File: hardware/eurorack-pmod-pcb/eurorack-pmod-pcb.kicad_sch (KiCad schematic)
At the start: 34 parts, among them J1 OPTIONAL, J2 PMOD, J3 EURORACK_PWR, U1 LM1117-3.3, U2 TL072, U3 AK4619VN

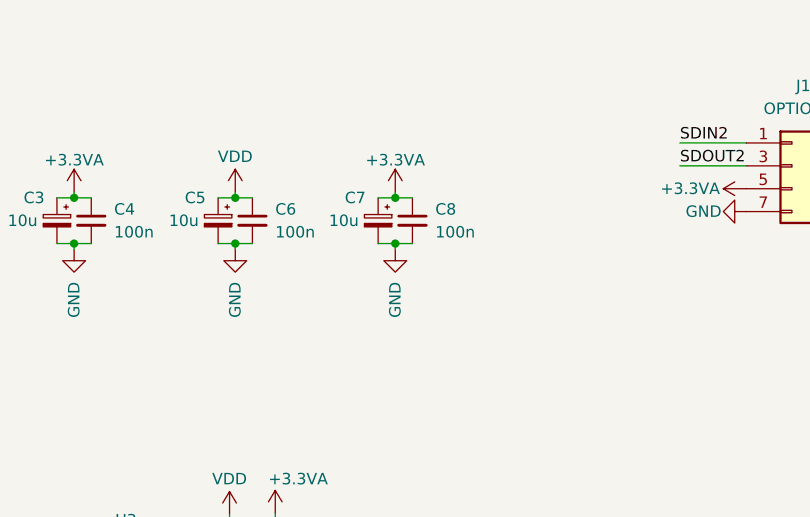
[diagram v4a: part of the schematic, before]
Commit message: Position all components on PCB
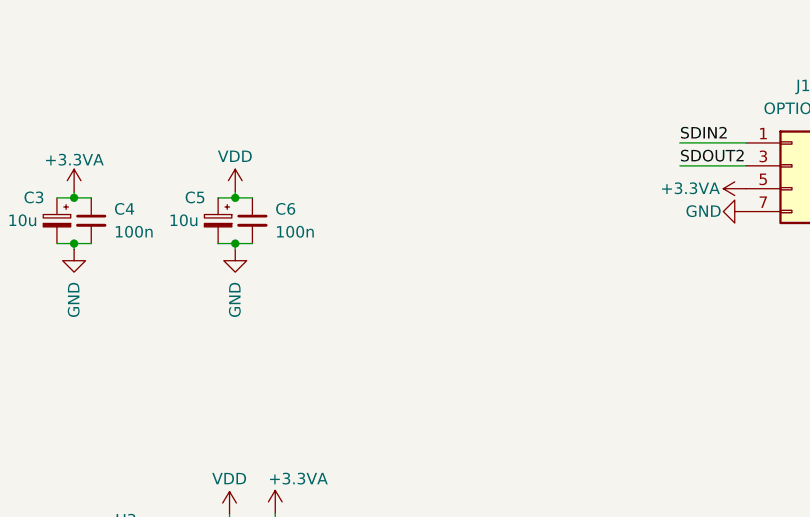
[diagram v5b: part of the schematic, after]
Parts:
- removed C7: 10u, Capacitor_Tantalum_SMD:CP_EIA-3216-10_Kemet-I, symbol Device:C_Polarized_Small
- removed C8: 100n, Capacitor_SMD:C_0603_1608Metric, symbol Device:C_Small
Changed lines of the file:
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@@
   (junction (at 247.015 88.9) (diameter 0) (color 0 0 0 0)
-  )
-  (junction (at 116.078 41.656) (diameter 0) (color 0 0 0 0)
-  )
-  (junction (at 116.078 36.576) (diameter 0) (color 0 0 0 0)
   )
   (junction (at 98.298 36.576) (diameter 0) (color 0 0 0 0)
@@
     (stroke (width 0) (type default) (color 0 0 0 0))
   )
-  (wire (pts (xy 116.078 41.656) (xy 117.983 41.656))
-    (stroke (width 0) (type default) (color 0 0 0 0))
-  )
   (wire (pts (xy 36.703 90.043) (xy 30.988 90.043))
     (stroke (width 0) (type default) (color 0 0 0 0))
@@
     (stroke (width 0) (type default) (color 0 0 0 0))
   )
-  (wire (pts (xy 116.078 41.656) (xy 116.078 42.291))
-    (stroke (width 0) (type default) (color 0 0 0 0))
-  )
   (wire (pts (xy 193.675 83.82) (xy 203.2 83.82))
     (stroke (width 0) (type default) (color 0 0 0 0))
@@
     (stroke (width 0) (type default) (color 0 0 0 0))
   )
-  (wire (pts (xy 114.173 41.656) (xy 116.078 41.656))
-    (stroke (width 0) (type default) (color 0 0 0 0))
-  )
   (wire (pts (xy 230.505 41.91) (xy 236.855 41.91))
     (stroke (width 0) (type default) (color 0 0 0 0))
@@
     (stroke (width 0) (type default) (color 0 0 0 0))
   )
-  (wire (pts (xy 116.078 35.941) (xy 116.078 36.576))
-    (stroke (width 0) (type default) (color 0 0 0 0))
-  )
   (wire (pts (xy 229.235 78.105) (xy 233.68 78.105))
     (stroke (width 0) (type default) (color 0 0 0 0))
@@
     (stroke (width 0) (type default) (color 0 0 0 0))
   )
-  (wire (pts (xy 116.078 36.576) (xy 117.983 36.576))
-    (stroke (width 0) (type default) (color 0 0 0 0))
-  )
   (wire (pts (xy 30.988 96.393) (xy 30.988 90.043))
     (stroke (width 0) (type default) (color 0 0 0 0))
@@
   )
   (wire (pts (xy 225.806 124.079) (xy 227.711 124.079))
-    (stroke (width 0) (type default) (color 0 0 0 0))
-  )
-  (wire (pts (xy 114.173 36.576) (xy 116.078 36.576))
     (stroke (width 0) (type default) (color 0 0 0 0))
   )
@@
     (pin "1")
   )
-  (symbol (lib_id "Device:C_Small") (at 117.983 39.116 0) (unit 1)
-    (in_bom yes) (on_board yes) (fields_autoplaced)
-    (property "Reference" "C8" (id 0) (at 120.523 37.8522 0)
-      (effects (font (size 1.27 1.27)) (justify left))
-    )
-    (property "Value" "100n" (id 1) (at 120.523 40.3922 0)
-      (effects (font (size 1.27 1.27)) (justify left))
-    )
-    (property "Footprint" "Capacitor_SMD:C_0603_1608Metric" (id 2) (at 117.983 39.116 0)
-      (effects (font (size 1.27 1.27)) hide)
-    )
-    (property "Datasheet" "~" (id 3) (at 117.983 39.116 0)
-      (effects (font (size 1.27 1.27)) hide)
-    )
-    (pin "1")
-    (pin "2")
-  )
   (symbol (lib_id "power:GND") (at 246.38 143.51 180) (unit 1)
     (in_bom yes) (on_board yes)
@@
     (pin "1")
   )
-  (symbol (lib_id "power:+3.3VA") (at 116.078 35.941 0) (unit 1)
-    (in_bom yes) (on_board yes)
-    (property "Reference" "#PWR015" (id 0) (at 116.078 39.751 0)
-      (effects (font (size 1.27 1.27)) hide)
-    )
-    (property "Value" "+3.3VA" (id 1) (at 116.078 32.385 0))
-    (property "Footprint" "" (id 2) (at 116.078 35.941 0)
-      (effects (font (size 1.27 1.27)) hide)
-    )
-    (property "Datasheet" "" (id 3) (at 116.078 35.941 0)
-      (effects (font (size 1.27 1.27)) hide)
-    )
-    (pin "1")
-  )
   (symbol (lib_id "power:GNDD") (at 69.723 137.16 0) (unit 1)
     (in_bom yes) (on_board yes) (fields_autoplaced)
@@
     )
     (property "Datasheet" "~" (id 3) (at 82.296 39.116 0)
-      (effects (font (size 1.27 1.27)) hide)
-    )
-    (pin "1")
-    (pin "2")
-  )
-  (symbol (lib_id "Device:C_Polarized_Small") (at 114.173 39.116 0) (mirror y) (unit 1)
-    (in_bom yes) (on_board yes)
-    (property "Reference" "C7" (id 0) (at 111.633 36.576 0))
-    (property "Value" "10u" (id 1) (at 110.363 39.116 0))
-    (property "Footprint" "Capacitor_Tantalum_SMD:CP_EIA-3216-10_Kemet-I" (id 2) (at 114.173 39.116 0)
-      (effects (font (size 1.27 1.27)) hide)
-    )
-    (property "Datasheet" "~" (id 3) (at 114.173 39.116 0)
       (effects (font (size 1.27 1.27)) hide)
     )
@@
     (pin "2")
   )
-  (symbol (lib_id "power:GND") (at 116.078 42.291 0) (unit 1)
-    (in_bom yes) (on_board yes)
-    (property "Reference" "#PWR024" (id 0) (at 116.078 48.641 0)
-      (effects (font (size 1.27 1.27)) hide)
-    )
-    (property "Value" "GND" (id 1) (at 116.078 49.911 90)
-      (effects (font (size 1.27 1.27)) (justify left))
-    )
-    (property "Footprint" "" (id 2) (at 116.078 42.291 0)
-      (effects (font (size 1.27 1.27)) hide)
-    )
-    (property "Datasheet" "" (id 3) (at 116.078 42.291 0)
-      (effects (font (size 1.27 1.27)) hide)
-    )
-    (pin "1")
-  )
   (symbol (lib_id "power:+5V") (at 29.718 27.813 0) (unit 1)
     (in_bom yes) (on_board yes)
@@
       (reference "#PWR014") (unit 1) (value "VDD") (footprint "")
     )
-    (path "/7c328871-126c-47c4-bbe2-7ab3ee8f32d9"
-      (reference "#PWR015") (unit 1) (value "+3.3VA") (footprint "")
-    )
     (path "/66c18ade-00b8-4d5b-9eb2-db4dc64dfd69"
       (reference "#PWR016") (unit 1) (value "GND") (footprint "")
@@
       (reference "#PWR023") (unit 1) (value "GND") (footprint "")
     )
-    (path "/be9d92df-8c25-476c-9086-b73d8a37ba62"
-      (reference "#PWR024") (unit 1) (value "GND") (footprint "")
-    )
     (path "/af64b9e9-cf6c-44d0-97a2-757f02f61370"
       (reference "#PWR025") (unit 1) (value "GND") (footprint "")
@@
       (reference "C6") (unit 1) (value "100n") (footprint "Capacitor_SMD:C_0603_1608Metric")
     )
-    (path "/8f1bdc56-2c2d-4f8a-98b2-fe5d783f2898"
-      (reference "C7") (unit 1) (value "10u") (footprint "Capacitor_Tantalum_SMD:CP_EIA-3216-10_Kemet-I")
-    )
-    (path "/6c62afb6-491a-48f3-b378-78e969fb1f38"
-      (reference "C8") (unit 1) (value "100n") (footprint "Capacitor_SMD:C_0603_1608Metric")
-    )
     (path "/04e44310-ac1a-4be8-8fdc-a71e796fa6bb"

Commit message: Finish routing
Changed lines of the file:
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@@
   (junction (at 227.711 129.159) (diameter 0) (color 0 0 0 0)
-  )
-  (junction (at 156.337 98.552) (diameter 0) (color 0 0 0 0)
   )
   (junction (at 227.711 124.079) (diameter 0) (color 0 0 0 0)
@@
   (junction (at 252.095 36.83) (diameter 0) (color 0 0 0 0)
   )
-  (junction (at 156.337 98.425) (diameter 0) (color 0 0 0 0)
-  )
   (junction (at 227.584 149.352) (diameter 0) (color 0 0 0 0)
   )
   (junction (at 229.235 86.36) (diameter 0) (color 0 0 0 0)
+  )
+  (junction (at 156.337 98.552) (diameter 0) (color 0 0 0 0)
   )
   (junction (at 263.525 29.21) (diameter 0) (color 0 0 0 0)
@@
   )
   (junction (at 29.718 34.671) (diameter 0) (color 0 0 0 0)
+  )
+  (junction (at 156.337 98.425) (diameter 0) (color 0 0 0 0)
   )
   (junction (at 227.584 144.272) (diameter 0) (color 0 0 0 0)
@@
     (stroke (width 0) (type default) (color 0 0 0 0))
   )
+  (wire (pts (xy 156.337 98.425) (xy 156.337 98.552))
+    (stroke (width 0) (type default) (color 0 0 0 0))
+  )
